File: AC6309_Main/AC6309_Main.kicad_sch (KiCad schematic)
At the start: 24 parts, among them J1 Address, J2 Data and Control, J3 FTDI Header, SW1 Reset, U1 HD63B09P, U2 W24257, U3 28C256, U4 HD63B50, U5 74HCT00, U6 74HC138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

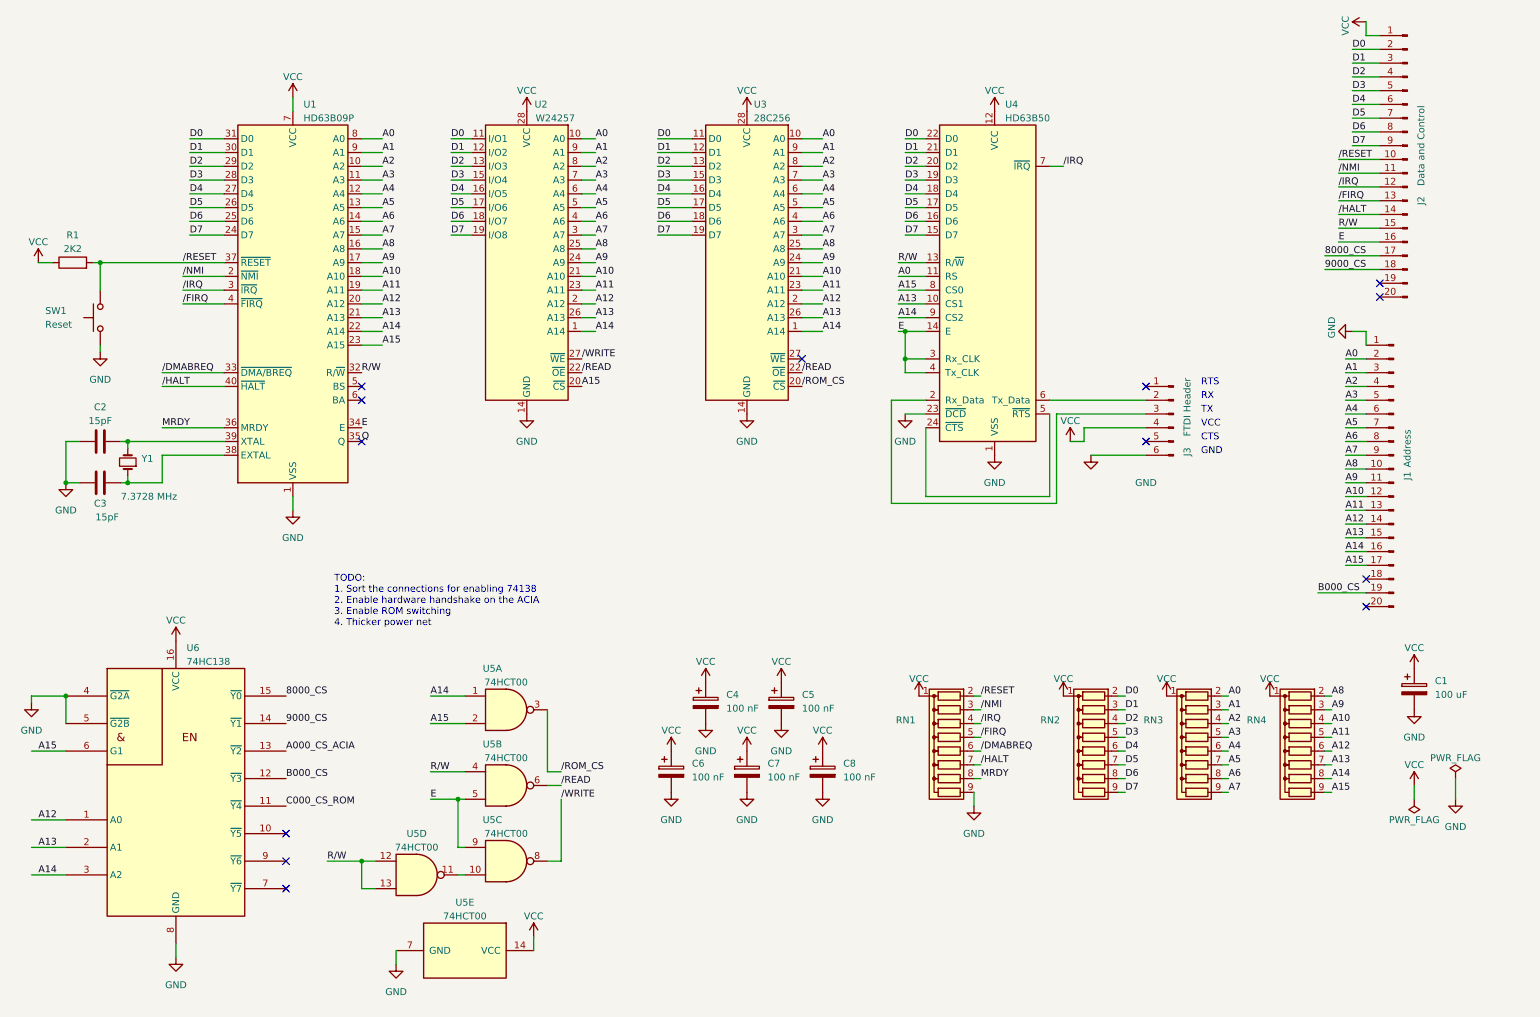
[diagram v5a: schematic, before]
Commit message: SCH and PCB updats. DRC issues fixed.
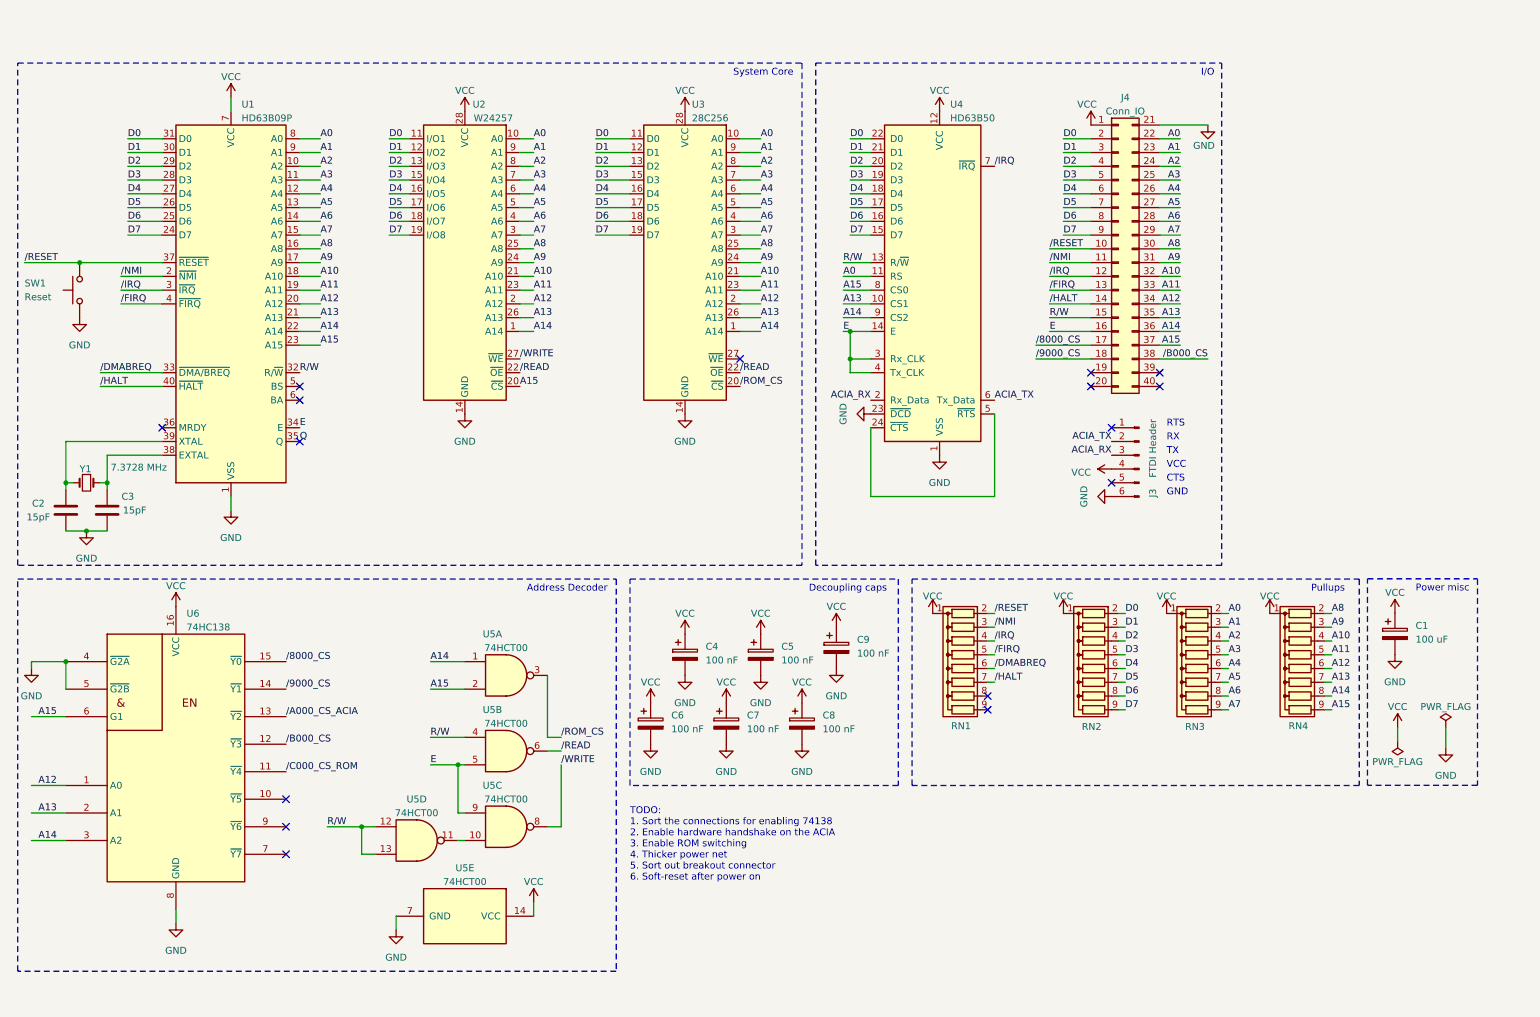
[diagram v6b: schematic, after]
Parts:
- removed J1: Address, Connector_PinHeader_2.54mm:PinHeader_1x20_P2.54mm_Vertical, symbol Connector:Conn_01x20_Pin
- removed J2: Data and Control, Connector_PinHeader_2.54mm:PinHeader_1x20_P2.54mm_Vertical, symbol Connector:Conn_01x20_Pin
- removed R1: 2K2, Resistor_THT:R_Axial_DIN0204_L3.6mm_D1.6mm_P2.54mm_Vertical, symbol Device:R
- added C9: 100 nF, Capacitor_THT:C_Disc_D3.0mm_W2.0mm_P2.50mm, symbol Device:C_Polarized
- added J4: Conn_IO, Connector_PinHeader_2.54mm:PinHeader_2x20_P2.54mm_Vertical, symbol Connector_Generic:Conn_02x20_Top_Bottom
- C1: footprint Capacitor_THT:CP_Radial_D4.0mm_P2.00mm -> Capacitor_THT:CP_Radial_D8.0mm_P2.50mm
- C4, C5, C6, C7, C8: footprint Capacitor_THT:CP_Radial_D4.0mm_P2.00mm -> Capacitor_THT:C_Disc_D3.0mm_W2.0mm_P2.50mm
- J3: footprint Connector_PinHeader_2.54mm:PinHeader_1x06_P2.54mm_Vertical -> Connector_PinSocket_2.54mm:PinSocket_1x06_P2.54mm_Vertical
- SW1: footprint Button_Switch_THT:SW_TH_Tactile_Omron_B3F-10xx -> Button_Switch_THT:SW_Tactile_Straight_KSL0Axx1LFTR
- U1: footprint Package_DIP:DIP-40_W15.24mm -> Package_DIP:DIP-40_W15.24mm_Socket
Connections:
- net A0: now also J4.22 (Pin_22)
- net A1: now also J4.23 (Pin_23)
- net A10: now also J4.32 (Pin_32)
- net A11: now also J4.33 (Pin_33)
- net A12: now also J4.34 (Pin_34)
- net A13: now also J4.35 (Pin_35)
- net A14: now also J4.36 (Pin_36)
- net A15: now also J4.37 (Pin_37)
- net A2: now also J4.24 (Pin_24)
- net A3: now also J4.25 (Pin_25)
- net A4: now also J4.26 (Pin_26)
- net A5: now also J4.27 (Pin_27)
- net A6: now also J4.28 (Pin_28)
- net A7: now also J4.29 (Pin_29)
- net A8: now also J4.30 (Pin_30)
- net A9: now also J4.31 (Pin_31)
- net D0: now also J4.2 (Pin_2)
- net D1: now also J4.3 (Pin_3)
- net D2: now also J4.4 (Pin_4)
- net D3: now also J4.5 (Pin_5)
- net D4: now also J4.6 (Pin_6)
- net D5: now also J4.7 (Pin_7)
- net D6: now also J4.8 (Pin_8)
- net D7: now also J4.9 (Pin_9)
- net E: now also J4.16 (Pin_16)
- net GND: now also C9.2, J4.21 (Pin_21); no longer RN1.9 (R8)
- net R/W: now also J4.15 (Pin_15)
- net VCC: now also C9.1, J4.1 (Pin_1)
- net /FIRQ: now also J4.13 (Pin_13)
- net /HALT: now also J4.14 (Pin_14)
- net /IRQ: now also J4.12 (Pin_12)
- net /NMI: now also J4.11 (Pin_11)
- net /RESET: now also J4.10 (Pin_10)
- net ACIA_TX: now reaches J3.2 (Pin_2), U4.6 (Tx_Data)
- net ACIA_RX: now reaches J3.3 (Pin_3), U4.2 (Rx_Data)
- net 8000_CS renamed /8000_CS
- net /8000_CS: now also J4.17 (Pin_17)
- net 9000_CS renamed /9000_CS
- net /9000_CS: now also J4.18 (Pin_18)
- net A000_CS_ACIA renamed /A000_CS_ACIA
- net B000_CS renamed /B000_CS
- net /B000_CS: now also J4.38 (Pin_38)
- net C000_CS_ROM renamed /C000_CS_ROM
- net MRDY: no longer names the net of RN1.8 (R7)
- net MRDY: no longer U1.36 (MRDY)
- no-connect marks 13 -> 16
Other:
- note added: "Address Decoder"
- note added: "Decoupling caps"
- note added: "I/O"
- note added: "Power misc"
- note added: "Pullups"
- note added: "System Core"
- note added: "TODO: 1. Sort the connections for enabling 74138 2. Enable hardware handshake on the ACIA 3. Enable ROM switching 4. Thicker power net 5. Sort out breakout connector 6. Soft-reset after power on"
- note removed: "TODO: 1. Sort the connections for enabling 74138 2. Enable hardware handshake on the ACIA 3. Enable ROM switching 4. Thicker power net"
- moved on the sheet: C1, C2, C3, C4, C5, C6, C7, C8, J3, RN1, RN2, RN3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

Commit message: Updates from 2024. Rev1 going in production.
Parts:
- renumbered J4 to J1, J3 to J2
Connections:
- net A0: now also J1.4 (Pin_4); no longer J1.22 (Pin_22)
- net A1: now also J1.6 (Pin_6); no longer J1.23 (Pin_23)
- net A10: now also J1.24 (Pin_24); no longer J1.32 (Pin_32)
- net A11: now also J1.26 (Pin_26); no longer J1.33 (Pin_33)
- net A12: now also J1.28 (Pin_28); no longer J1.34 (Pin_34)
- net A13: now also J1.30 (Pin_30); no longer J1.35 (Pin_35)
- net A14: now also J1.32 (Pin_32); no longer J1.36 (Pin_36)
- net A15: now also J1.34 (Pin_34); no longer J1.37 (Pin_37)
- net A2: now also J1.8 (Pin_8); no longer J1.24 (Pin_24)
- net A3: now also J1.10 (Pin_10); no longer J1.25 (Pin_25)
- net A4: now also J1.12 (Pin_12); no longer J1.26 (Pin_26)
- net A5: now also J1.14 (Pin_14); no longer J1.27 (Pin_27)
- net A6: now also J1.16 (Pin_16); no longer J1.28 (Pin_28)
- net A7: now also J1.18 (Pin_18); no longer J1.29 (Pin_29)
- net A8: now also J1.20 (Pin_20); no longer J1.30 (Pin_30)
- net A9: now also J1.22 (Pin_22); no longer J1.31 (Pin_31)
- net ACIA_RX: now also J2.2 (Pin_2); no longer J2.3 (Pin_3)
- net ACIA_TX: now also J2.3 (Pin_3); no longer J2.2 (Pin_2)
- net D0: now also J1.3 (Pin_3); no longer J1.2 (Pin_2)
- net D1: now also J1.5 (Pin_5); no longer J1.3 (Pin_3)
- net D2: now also J1.7 (Pin_7); no longer J1.4 (Pin_4)
- net D3: now also J1.9 (Pin_9); no longer J1.5 (Pin_5)
- net D4: now also J1.11 (Pin_11); no longer J1.6 (Pin_6)
- net D5: now also J1.13 (Pin_13); no longer J1.7 (Pin_7)
- net D6: now also J1.15 (Pin_15); no longer J1.8 (Pin_8)
- net D7: now also J1.17 (Pin_17); no longer J1.9 (Pin_9)
- net E: now also J1.31 (Pin_31); no longer J1.16 (Pin_16)
- net GND: now also J1.2 (Pin_2); no longer J1.21 (Pin_21)
- net R/W: now also J1.29 (Pin_29); no longer J1.15 (Pin_15)
- net /8000_CS: now also J1.33 (Pin_33); no longer J1.17 (Pin_17)
- net /9000_CS: now also J1.35 (Pin_35); no longer J1.18 (Pin_18)
- net /B000_CS: now also J1.36 (Pin_36); no longer J1.38 (Pin_38)
- net /DMABREQ: now also RN1.7 (R6); no longer RN1.6 (R5)
- net /FIRQ: now also J1.25 (Pin_25); no longer J1.13 (Pin_13)
- net /HALT: now also J1.27 (Pin_27), RN1.6 (R5); no longer J1.14 (Pin_14), RN1.7 (R6)
- net /IRQ: now also J1.23 (Pin_23); no longer J1.12 (Pin_12)
- net /NMI: now also J1.21 (Pin_21); no longer J1.11 (Pin_11)
- net /RESET: now also J1.19 (Pin_19); no longer J1.10 (Pin_10)
- net Q: no longer names the net of U1.35 (Q)
- net /C000_CS_ROM: no longer names the net of U6.11 (~{Y4})
- no-connect marks 16 -> 17
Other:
- note added: "ACIA"
- note added: "Address Decoding"
- note added: "Address space TO BE: $0000-$7FFF RAM 32K $8000-$9FFF Extended RAM 8K $A000-$AFFF Internal devices (UART,SPI,I2C) $B000-$BFFF External devices (Port1,Port2,Port3) $C000-$FFFF 8K ROM"
- note added: "Address space: $0000-$7FFF RAM $8000-$8FFF Extension port #1 $9000-$9FFF Extension port #2 $A000-$AFFF UART $B000-$BFFF Extension port #3 $C000-$FFFF ROM"
- note added: "Connectors"
- note added: "Core"
- note added: "TODO: 0. Rework ACIA selection (use /A000_ACIA_CS) 1. Enable hardware handshake on the ACIA 2. Enable ROM switching"
- note removed: "Address Decoder"
- note removed: "I/O"
- note removed: "System Core"
- note removed: "TODO: 1. Sort the connections for enabling 74138 2. Enable hardware handshake on the ACIA 3. Enable ROM switching 4. Thicker power net 5. Sort out breakout connector 6. Soft-reset after power on"
- moved on the sheet: C1, J1, J2, RN1, RN2, RN3, RN4, U2, U3, U4, U5A, U5B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
